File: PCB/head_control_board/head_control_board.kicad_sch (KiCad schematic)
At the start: 62 parts, among them Q1 AO3401A, U1 TPS63070RNMR, U2 TPS63070RNMR, U3 SN74AHCT245PWR, U4 ESP32-S3-WROOM-1(N16R8)

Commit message: Finish component selection
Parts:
- R10, R11: LCSC Part C60491 -> C25741
- R13: value 60 -> 68; LCSC Part C865587 -> C17802
- R15, R16: LCSC Part C115337 -> C27834
- R6: footprint Resistor_SMD:R_0402_1005Metric -> Resistor_SMD:R_0603_1608Metric; LCSC Part C163456 -> C25822
- R7: footprint Resistor_SMD:R_0402_1005Metric -> Resistor_SMD:R_0603_1608Metric; LCSC Part C25790 -> C23178
- R8: footprint Resistor_SMD:R_0402_1005Metric -> Resistor_SMD:R_0603_1608Metric; LCSC Part C93946 -> C22795
- R9: footprint Resistor_SMD:R_0402_1005Metric -> Resistor_SMD:R_0603_1608Metric; LCSC Part C25755 -> C22807
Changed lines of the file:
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@@
 			)
 		)
-		(property "LCSC Part" "C115337"
+		(property "LCSC Part" "C27834"
 			(at 29.21 34.29 0)
 			(effects
@@
 			)
 		)
-		(property "Value" "60"
+		(property "Value" "68"
 			(at 273.05 36.576 90)
 			(effects
@@
 			)
 		)
-		(property "LCSC Part" "C865587"
+		(property "LCSC Part" "C17802"
 			(at 270.51 34.29 0)
 			(effects
@@
 			)
 		)
-		(property "Footprint" "Resistor_SMD:R_0402_1005Metric"
+		(property "Footprint" "Resistor_SMD:R_0603_1608Metric"
 			(at 137.16 140.462 90)
 			(effects
@@
 			)
 		)
-		(property "LCSC Part" "C25755"
+		(property "LCSC Part" "C22807"
 			(at 137.16 142.24 0)
 			(effects
@@
 			)
 		)
-		(property "LCSC Part" "C60491"
+		(property "LCSC Part" "C25741"
 			(at 153.67 142.24 0)
 			(effects
@@
 			)
 		)
-		(property "Footprint" "Resistor_SMD:R_0402_1005Metric"
+		(property "Footprint" "Resistor_SMD:R_0603_1608Metric"
 			(at 130.048 88.9 90)
 			(effects
@@
 			)
 		)
-		(property "LCSC Part" "C163456"
+		(property "LCSC Part" "C25822"
 			(at 128.27 88.9 0)
 			(effects
@@
 			)
 		)
-		(property "Footprint" "Resistor_SMD:R_0402_1005Metric"
+		(property "Footprint" "Resistor_SMD:R_0603_1608Metric"
 			(at 130.048 137.16 90)
 			(effects
@@
 			)
 		)
-		(property "LCSC Part" "C25790"
+		(property "LCSC Part" "C23178"
 			(at 128.27 137.16 0)
 			(effects
@@
 			)
 		)
-		(property "LCSC Part" "C60491"
+		(property "LCSC Part" "C25741"
 			(at 153.67 93.98 0)
 			(effects
@@
 			)
 		)
-		(property "Footprint" "Resistor_SMD:R_0402_1005Metric"
+		(property "Footprint" "Resistor_SMD:R_0603_1608Metric"
 			(at 137.16 92.202 90)
 			(effects
@@
 			)
 		)
-		(property "LCSC Part" "C93946"
+		(property "LCSC Part" "C22795"
 			(at 137.16 93.98 0)
 			(effects
@@
 			)
 		)
-		(property "LCSC Part" "C115337"
+		(property "LCSC Part" "C27834"
 			(at 29.21 31.75 0)
 			(effects

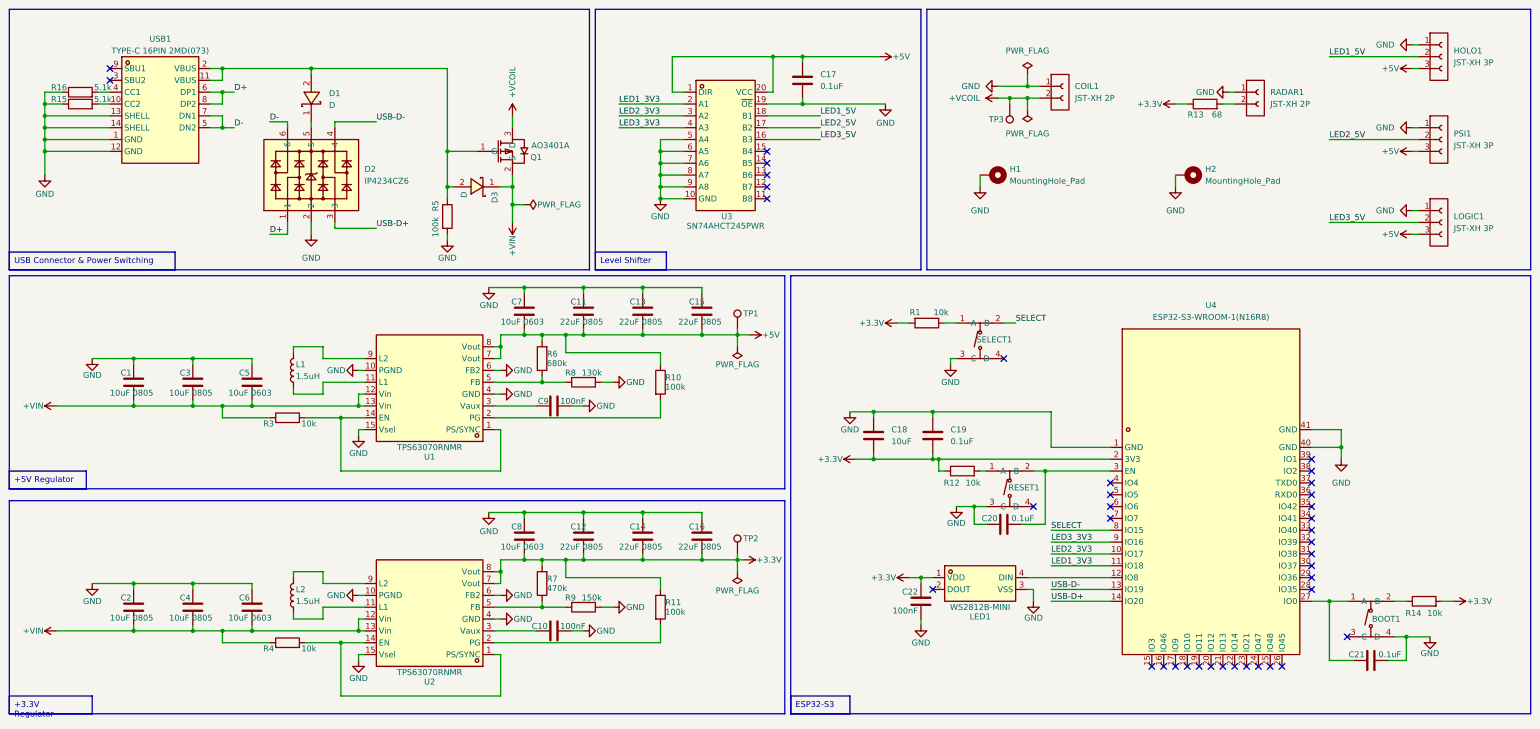
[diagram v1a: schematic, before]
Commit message: Component cost optimization
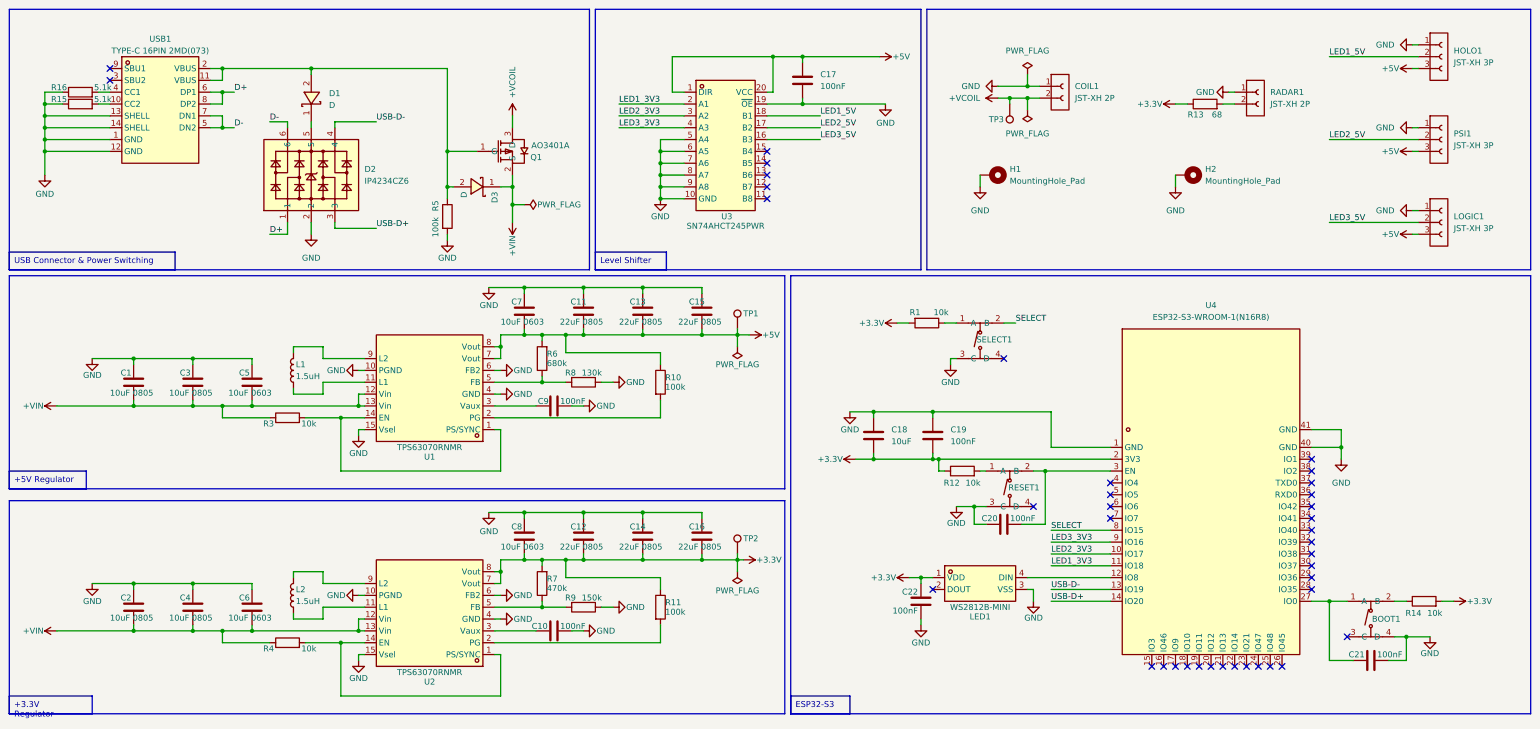
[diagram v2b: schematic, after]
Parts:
- BOOT1, RESET1, SELECT1: footprint LCSC:SW-SMD_4P-L5.1-W5.1-P3.70-LS6.5-TL-2 -> LCSC:SW-SMD_4P-L5.2-W5.2-P3.70-LS6.4; LCSC Part C318884 -> (none)
- C17: value 0.1uF -> 100nF; footprint Capacitor_SMD:C_0805_2012Metric -> Capacitor_SMD:C_0402_1005Metric; LCSC Part C49678 -> C307331
- C19, C20, C21: value 0.1uF -> 100nF; footprint Capacitor_SMD:C_0603_1608Metric -> Capacitor_SMD:C_0402_1005Metric; LCSC Part C14663 -> C307331
- R1, R12, R14: footprint Resistor_SMD:R_0805_2012Metric -> Resistor_SMD:R_0402_1005Metric; LCSC Part C17414 -> C25744
- R13: footprint Resistor_SMD:R_0805_2012Metric -> Resistor_THT:R_Axial_DIN0207_L6.3mm_D2.5mm_P7.62mm_Horizontal; LCSC Part C17802 -> (none)
- R5: footprint Resistor_SMD:R_0805_2012Metric -> Resistor_SMD:R_0402_1005Metric; LCSC Part C149504 -> C25741
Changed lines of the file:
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@@
 			)
 		)
-		(property "Footprint" "Resistor_SMD:R_0805_2012Metric"
+		(property "Footprint" "Resistor_SMD:R_0402_1005Metric"
 			(at 106.172 58.42 90)
 			(effects
@@
 			)
 		)
-		(property "LCSC Part" "C149504"
+		(property "LCSC Part" "C25741"
 			(at 107.95 58.42 0)
 			(effects
@@
 			)
 		)
-		(property "Footprint" "Resistor_SMD:R_0805_2012Metric"
+		(property "Footprint" "Resistor_SMD:R_0402_1005Metric"
 			(at 218.44 114.808 90)
 			(effects
@@
 			)
 		)
-		(property "LCSC Part" "C17414"
+		(property "LCSC Part" "C25744"
 			(at 218.44 113.03 0)
 			(effects
@@
 			)
 		)
-		(property "Value" "0.1uF"
+		(property "Value" "100nF"
 			(at 231.394 123.19 90)
 			(effects
@@
 			)
 		)
-		(property "Footprint" "Capacitor_SMD:C_0603_1608Metric"
+		(property "Footprint" "Capacitor_SMD:C_0402_1005Metric"
 			(at 231.14 123.4948 0)
 			(effects
@@
 			)
 		)
-		(property "LCSC Part" "C14663"
+		(property "LCSC Part" "C307331"
 			(at 227.33 124.46 0)
 			(effects
@@
 			)
 		)
-		(property "Footprint" "Resistor_SMD:R_0805_2012Metric"
+		(property "Footprint" "Resistor_THT:R_Axial_DIN0207_L6.3mm_D2.5mm_P7.62mm_Horizontal"
 			(at 270.51 36.068 90)
 			(effects
@@
 			)
 		)
-		(property "LCSC Part" "C17802"
+		(property "LCSC Part" ""
 			(at 270.51 34.29 0)
 			(effects
@@
 			)
 		)
-		(property "Value" "0.1uF"
+		(property "Value" "100nF"
 			(at 187.96 30.4799 0)
 			(effects
@@
 			)
 		)
-		(property "Footprint" "Capacitor_SMD:C_0805_2012Metric"
+		(property "Footprint" "Capacitor_SMD:C_0402_1005Metric"
 			(at 183.1848 25.4 0)
 			(effects
@@
 			)
 		)
-		(property "LCSC Part" "C49678"
+		(property "LCSC Part" "C307331"
 			(at 184.15 29.21 0)
 			(effects
@@
 			)
 		)
-		(property "Value" "0.1uF"
+		(property "Value" "100nF"
 			(at 215.9 106.6799 0)
 			(effects
@@
 			)
 		)
-		(property "Footprint" "Capacitor_SMD:C_0603_1608Metric"
+		(property "Footprint" "Capacitor_SMD:C_0402_1005Metric"
 			(at 213.0552 109.22 0)
 			(effects
@@
 			)
 		)
-		(property "LCSC Part" "C14663"
+		(property "LCSC Part" "C307331"
 			(at 212.09 105.41 0)
 			(effects
@@
 			)
 		)
-		(property "Footprint" "LCSC:SW-SMD_4P-L5.1-W5.1-P3.70-LS6.5-TL-2"
+		(property "Footprint" "LCSC:SW-SMD_4P-L5.2-W5.2-P3.70-LS6.4"
 			(at 228.6 128.27 0)
 			(effects
@@
 			)
 		)
-		(property "LCSC Part" "C318884"
+		(property "LCSC Part" ""
 			(at 228.6 133.35 0)
 			(effects
@@
 			)
 		)
-		(property "Footprint" "Resistor_SMD:R_0805_2012Metric"
+		(property "Footprint" "Resistor_SMD:R_0402_1005Metric"
 			(at 317.5 142.748 90)
 			(effects
@@
 			)
 		)
-		(property "LCSC Part" "C17414"
+		(property "LCSC Part" "C25744"
 			(at 317.5 140.97 0)
 			(effects
@@
 			)
 		)
-		(property "Footprint" "LCSC:SW-SMD_4P-L5.1-W5.1-P3.70-LS6.5-TL-2"
+		(property "Footprint" "LCSC:SW-SMD_4P-L5.2-W5.2-P3.70-LS6.4"
 			(at 306.07 156.21 0)
 			(effects
@@
 			)
 		)
-		(property "LCSC Part" "C318884"
+		(property "LCSC Part" ""
 			(at 306.07 161.29 0)
 			(effects
@@
 			)
 		)
-		(property "Footprint" "LCSC:SW-SMD_4P-L5.1-W5.1-P3.70-LS6.5-TL-2"
+		(property "Footprint" "LCSC:SW-SMD_4P-L5.2-W5.2-P3.70-LS6.4"
 			(at 222.25 96.52 0)
 			(effects
@@
 			)
 		)
-		(property "LCSC Part" "C318884"
+		(property "LCSC Part" ""
 			(at 222.25 101.6 0)
 			(effects
@@
 			)
 		)
-		(property "Footprint" "Resistor_SMD:R_0805_2012Metric"
+		(property "Footprint" "Resistor_SMD:R_0402_1005Metric"
 			(at 210.82 79.502 90)
 			(effects
@@
 			)
 		)
-		(property "LCSC Part" "C17414"
+		(property "LCSC Part" "C25744"
 			(at 210.82 81.28 0)
 			(effects
@@
 			)
 		)
-		(property "Value" "0.1uF"
+		(property "Value" "100nF"
 			(at 310.134 152.4 90)
 			(effects
@@
 			)
 		)
-		(property "Footprint" "Capacitor_SMD:C_0603_1608Metric"
+		(property "Footprint" "Capacitor_SMD:C_0402_1005Metric"
 			(at 309.88 152.7048 0)
 			(effects
@@
 			)
 		)
-		(property "LCSC Part" "C14663"
+		(property "LCSC Part" "C307331"
 			(at 306.07 153.67 0)
 			(effects

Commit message: Rev 1.0 boards ordered
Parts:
- BOOT1, COIL1, HOLO1, LOGIC1, PSI1, R13, RADAR1, RESET1, SELECT1: now left out of the parts list
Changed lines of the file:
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@@
 		(unit 1)
 		(exclude_from_sim no)
-		(in_bom yes)
+		(in_bom no)
 		(on_board yes)
 		(dnp no)
@@
 		(unit 1)
 		(exclude_from_sim no)
-		(in_bom yes)
+		(in_bom no)
 		(on_board yes)
 		(dnp no)
@@
 		(unit 1)
 		(exclude_from_sim no)
-		(in_bom yes)
+		(in_bom no)
 		(on_board yes)
 		(dnp no)
@@
 		(unit 1)
 		(exclude_from_sim no)
-		(in_bom yes)
+		(in_bom no)
 		(on_board yes)
 		(dnp no)
@@
 		(unit 1)
 		(exclude_from_sim no)
-		(in_bom yes)
+		(in_bom no)
 		(on_board yes)
 		(dnp no)
@@
 		(unit 1)
 		(exclude_from_sim no)
-		(in_bom yes)
+		(in_bom no)
 		(on_board yes)
 		(dnp no)
@@
 		(unit 1)
 		(exclude_from_sim no)
-		(in_bom yes)
+		(in_bom no)
 		(on_board yes)
 		(dnp no)
@@
 		(unit 1)
 		(exclude_from_sim no)
-		(in_bom yes)
+		(in_bom no)
 		(on_board yes)
 		(dnp no)
@@
 		(unit 1)
 		(exclude_from_sim no)
-		(in_bom yes)
+		(in_bom no)
 		(on_board yes)
 		(dnp no)
